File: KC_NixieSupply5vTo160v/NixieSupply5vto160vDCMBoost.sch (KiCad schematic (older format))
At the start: 47 parts, among them J1 Screw_Terminal_1x04, J2 CONN_01X01, J3 CONN_01X01, J4 CONN_01X01, J5 CONN_01X01, P1 USB_OTG, Q1 FDS2672CT, Q26 MMBTA42, U1 UCC3803

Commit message: Flyback Efficiency Calculations
Added a Efficiency calculations for a flyback converter using similar
parts, but with an off the self 8.5uH 1:5 turns ration flyback
transformer.  the DCM boost still looks like the highest efficiency.
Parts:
- removed J1: Screw_Terminal_1x04, TerminalBlock_Phoenix:TerminalBlock_Phoenix_PT-3.5mm_4pol, symbol Screw_Terminal_1x04
- removed P1: USB_OTG, NixieSupply5vto160vDCMBoost_socket:USB_Micro-B_Wurth_3A_Non-OVAL-Drill, symbol USB_OTG-RESCUE-ETAclock
- added J1: Screw_Terminal_01x04, TerminalBlock_Phoenix:TerminalBlock_Phoenix_PT-3.5mm_4pol, symbol Screw_Terminal_01x04
- added P1: USB_OTG, NixieSupply5vto160vDCMBoost_socket:USB_Micro-B_Wurth_3A_Non-OVAL-Drill, symbol USB_OTG
- J2, J3, J4, J5: symbol CONN_01X01 -> Conn_01x01
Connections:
- wire segments 161 -> 125

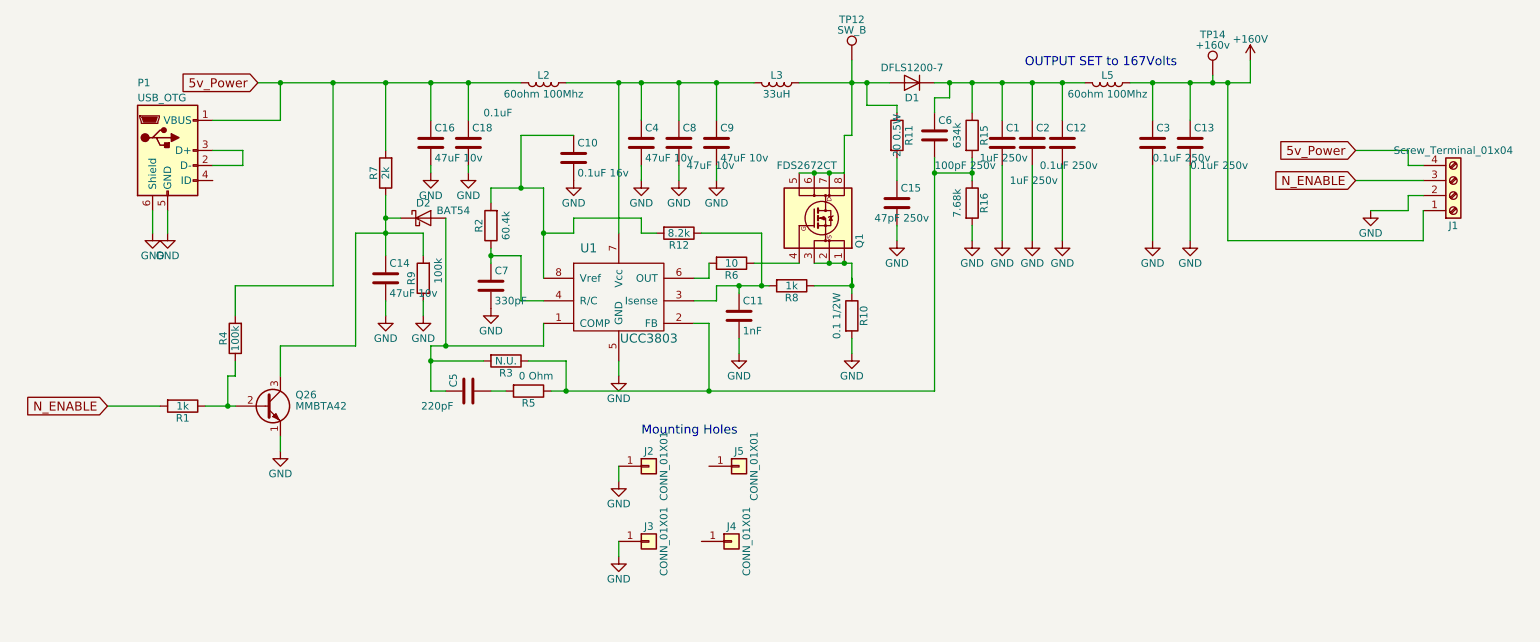
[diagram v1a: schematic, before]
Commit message: Latest updates for the verification Blog
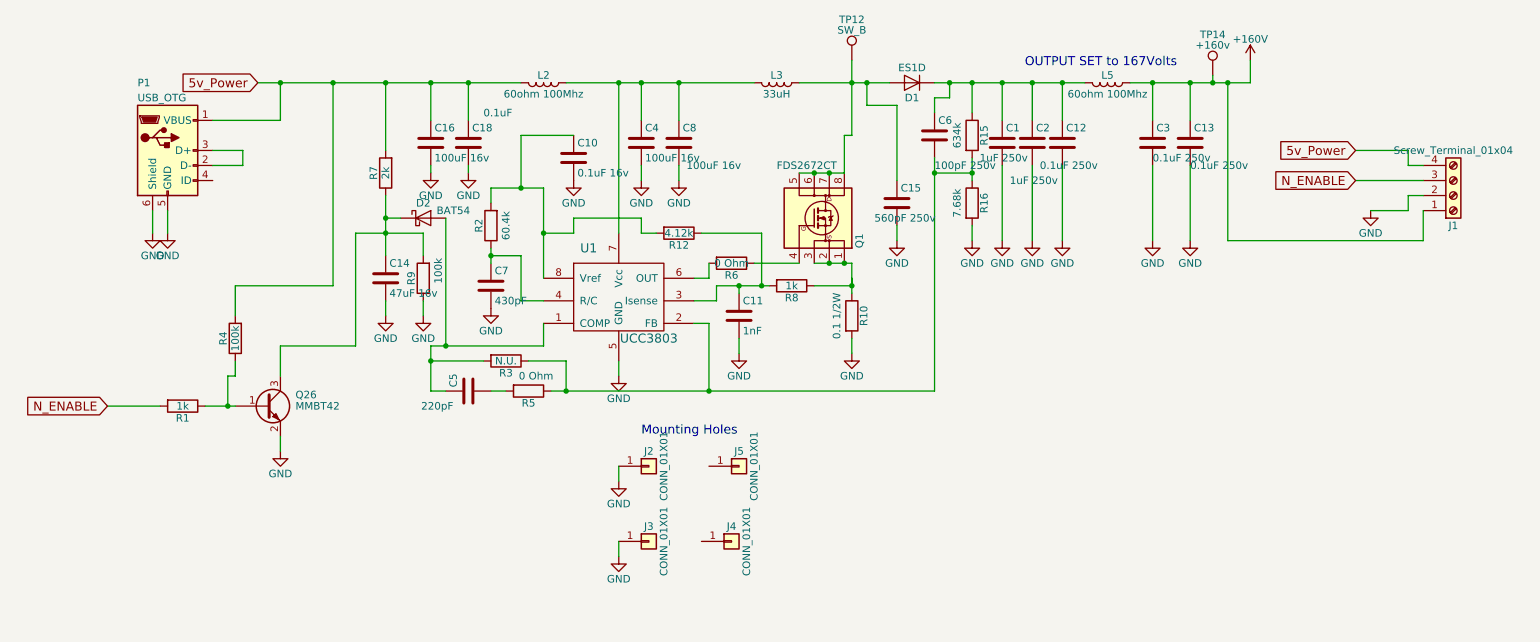
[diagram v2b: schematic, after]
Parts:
- removed C9: 47uF 10v, Capacitors_SMD:C_0805, symbol C
- removed Q26: MMBTA42, TO_SOT_Packages_SMD:SOT-23, symbol MPSA42
- removed R11: 20 0.5W, Resistors_SMD:R_0805, symbol R
- added Q26: MMBT42, TO_SOT_Packages_SMD:SOT-23, symbol MMBT3904
- C12, C13, C3, C6: MPN (none) -> CGA4J3X7T2E104M125AE
- C14: value 47uF 10v -> 47uF 16v; footprint Capacitors_SMD:C_0805 -> Capacitors_SMD:C_1206; MPN GRM21BR61A476ME15L -> C3216JB1C476M160AB
- C15: value 47pF 250v -> 560pF 250v; MPN C1608C0G2E331J080AA -> C0603C561JAGAC7867
- C16, C4, C8: value 47uF 10v -> 100uF 16v; footprint Capacitors_SMD:C_0805 -> Capacitors_SMD:C_1210; MPN GRM21BR61A476ME15L -> EMK325ABJ107MM-P
- C7: value 330pF -> 430pF; MPN (none) -> CL21C431JBANNNC
- D1: value DFLS1200-7 -> ES1D; footprint Diodes_SMD:D_PowerDI-123 -> Diodes_SMD:D_SMA_Handsoldering; MPN DFLS1200-7 -> ES1D
- J1: MPN (none) -> 1984633
- R12: value 8.2k -> 4.12k
- R6: value 10 -> 0 Ohm
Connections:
- net GND: now also Q26.2 (E)
- net at D1.2 (A), L3.1, Q1.5 (D)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: now also C15.1
- net at R1.1, R4.1: now also Q26.1 (B)
- net at C14.1, D2.1 (K), R7.1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: now also Q26.3 (C)
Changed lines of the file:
@@
 EELAYER 25 0
 EELAYER END
-$Descr A4 11693 8268
+$Descr USLetter 11000 8500
 encoding utf-8
 Sheet 1 1
@@
 P 6550 2050
 F 0 "D1" H 6550 2150 50  0000 C CNN
-F 1 "DFLS1200-7" H 6550 1950 50  0000 C CNN
-F 2 "Diodes_SMD:D_PowerDI-123" H 6550 2050 50  0001 C CNN
-F 3 "https://www.digikey.com/product-detail/en/diodes-incorporated/DFLS1200-7/DFLS1200DITR-ND/776776" H 6550 2050 50  0001 C CNN
-F 4 "DFLS1200-7 " H 6550 2050 60  0001 C CNN "MPN"
+F 1 "ES1D" H 6550 1950 50  0000 C CNN
+F 2 "Diodes_SMD:D_SMA_Handsoldering" H 6550 2050 50  0001 C CNN
+F 3 "https://www.digikey.com/product-detail/en/on-semiconductor/ES1D/ES1DFSCT-ND/458940" H 6550 2050 50  0001 C CNN
+F 4 "ES1D" H 6550 2050 60  0001 C CNN "MPN"
 	1    6550 2050
 	-1   0    0    1
@@
 P 5350 3250
 F 0 "R6" V 5430 3250 50  0000 C CNN
-F 1 "10" V 5350 3250 50  0000 C CNN
+F 1 "0 Ohm" V 5350 3250 50  0000 C CNN
 F 2 "Resistors_SMD:R_0805" V 5280 3250 50  0001 C CNN
 F 3 "" H 5350 3250 50  0000 C CNN
@@
 $EndComp
 $Comp
-L R R11
-U 1 1 58854C64
-P 6450 2400
-F 0 "R11" V 6530 2400 50  0000 C CNN
-F 1 "20 0.5W" V 6450 2400 50  0000 C CNN
-F 2 "Resistors_SMD:R_0805" V 6380 2400 50  0001 C CNN
-F 3 "" H 6450 2400 50  0001 C CNN
-	1    6450 2400
-	1    0    0    -1
-$EndComp
-$Comp
 L C C15
 U 1 1 58854D96
 P 6450 2850
 F 0 "C15" H 6475 2950 50  0000 L CNN
-F 1 "47pF 250v" H 6300 2750 50  0000 L CNN
+F 1 "560pF 250v" H 6300 2750 50  0000 L CNN
 F 2 "Capacitors_SMD:C_0603" H 6488 2700 50  0001 C CNN
-F 3 "http://www.digikey.com/product-detail/en/tdk-corporation/C1608C0G2E331J080AA/445-2317-1-ND/789826" H 6450 2850 50  0001 C CNN
-F 4 "C1608C0G2E331J080AA" H 6450 2850 60  0001 C CNN "MPN"
+F 3 "https://www.digikey.com/product-detail/en/kemet/C0603C561JAGAC7867/399-14990-1-ND/7382539" H 6450 2850 50  0001 C CNN
+F 4 "C0603C561JAGAC7867" H 6450 2850 60  0001 C CNN "MPN"
 	1    6450 2850
 	1    0    0    -1
@@
 P 3750 3400
 F 0 "C7" H 3775 3500 50  0000 L CNN
-F 1 "330pF" H 3775 3300 50  0000 L CNN
+F 1 "430pF" H 3775 3300 50  0000 L CNN
 F 2 "Capacitors_SMD:C_0805" H 3788 3250 50  0001 C CNN
-F 3 "" H 3750 3400 50  0000 C CNN
+F 3 "https://www.digikey.com/product-detail/en/samsung-electro-mechanics/CL21C431JBANNNC/1276-2659-1-ND/3890745" H 3750 3400 50  0001 C CNN
+F 4 "CL21C431JBANNNC" H 3750 3400 60  0001 C CNN "MPN"
 	1    3750 3400
 	1    0    0    -1
@@
 F 1 "100pF 250v" H 6700 2200 50  0000 L CNN
 F 2 "Capacitors_SMD:C_0805" H 6738 2250 50  0001 C CNN
-F 3 "" H 6700 2400 50  0000 C CNN
+F 3 "https://www.digikey.com/scripts/DkSearch/dksus.dll?Detail&itemSeq=248804877&uq=636513106927966714" H 6700 2400 50  0001 C CNN
+F 4 "CGA4J3X7T2E104M125AE" H 6700 2400 60  0001 C CNN "MPN"
 	1    6700 2400
 	1    0    0    -1
@@
 Connection ~ 6950 2650
 Wire Wire Line
-	6450 2700 6450 2550
-Wire Wire Line
-	6450 2200 6450 2250
+	6450 2200 6450 2700
 Wire Wire Line
 	6250 2200 6450 2200
@@
 	5000 2600 5000 2700
 $Comp
-L C C9
-U 1 1 5A46B83F
-P 5250 2450
-F 0 "C9" H 5275 2550 50  0000 L CNN
-F 1 "47uF 10v" H 5275 2350 50  0000 L CNN
-F 2 "Capacitors_SMD:C_0805" H 5288 2300 50  0001 C CNN
-F 3 "http://www.digikey.com/product-detail/en/murata-electronics-north-america/GRM21BR61A476ME15L/490-9961-1-ND/5026442" H 5250 2450 50  0001 C CNN
-F 4 "GRM21BR61A476ME15L" H 5250 2450 60  0001 C CNN "MPN"
-	1    5250 2450
-	1    0    0    -1
-$EndComp
-Wire Wire Line
-	5250 2300 5250 2050
-Connection ~ 5250 2050
-$Comp
-L GND #PWR023
-U 1 1 5A46B995
-P 5250 2700
-F 0 "#PWR023" H 5250 2450 50  0001 C CNN
-F 1 "GND" H 5250 2550 50  0000 C CNN
-F 2 "" H 5250 2700 50  0000 C CNN
-F 3 "" H 5250 2700 50  0000 C CNN
-	1    5250 2700
-	1    0    0    -1
-$EndComp
-Wire Wire Line
-	5250 2600 5250 2700
-$Comp
 L Conn_01x01 J5
 U 1 1 5A46B464
@@
 	4600 5200 4600 5100
 $Comp
-L GND #PWR024
+L GND #PWR023
 U 1 1 5A47271C
 P 4600 5200
-F 0 "#PWR024" H 4600 4950 50  0001 C CNN
+F 0 "#PWR023" H 4600 4950 50  0001 C CNN
 F 1 "GND" H 4600 5050 50  0000 C CNN
 F 2 "" H 4600 5200 50  0000 C CNN
@@
 $EndComp
 $Comp
-L GND #PWR025
+L GND #PWR024
 U 1 1 5A4727AE
 P 4600 4700
-F 0 "#PWR025" H 4600 4450 50  0001 C CNN
+F 0 "#PWR024" H 4600 4450 50  0001 C CNN
 F 1 "GND" H 4600 4550 50  0000 C CNN
 F 2 "" H 4600 4700 50  0000 C CNN
@@
 $EndComp
 $Comp
-L GND #PWR026
+L GND #PWR025
 U 1 1 5A4786FA
 P 4300 2700
-F 0 "#PWR026" H 4300 2450 50  0001 C CNN
+F 0 "#PWR025" H 4300 2450 50  0001 C CNN
 F 1 "GND" H 4300 2550 50  0000 C CNN
 F 2 "" H 4300 2700 50  0000 C CNN
@@
 P 5000 3050
 F 0 "R12" V 5080 3050 50  0000 C CNN
-F 1 "8.2k" V 5000 3050 50  0000 C CNN
+F 1 "4.12k" V 5000 3050 50  0000 C CNN
 F 2 "Resistors_SMD:R_0805" V 4930 3050 50  0001 C CNN
 F 3 "" H 5000 3050 50  0000 C CNN
@@
 F 1 "0.1uF 250v" H 8400 2300 50  0000 L CNN
 F 2 "Capacitors_SMD:C_0805" H 8438 2300 50  0001 C CNN
-F 3 "" H 8400 2450 50  0000 C CNN
+F 3 "https://www.digikey.com/product-detail/en/tdk-corporation/CGA4J3X7T2E104M125AE/445-7965-1-ND/2782533" H 8400 2450 50  0001 C CNN
+F 4 "CGA4J3X7T2E104M125AE" H 8400 2450 60  0001 C CNN "MPN"
 	1    8400 2450
 	1    0    0    -1
@@
 F 1 "0.1uF 250v" H 8150 2350 50  0000 L CNN
 F 2 "Capacitors_SMD:C_0805" H 8188 2300 50  0001 C CNN
-F 3 "" H 8150 2450 50  0000 C CNN
+F 3 "https://www.digikey.com/product-detail/en/tdk-corporation/CGA4J3X7T2E104M125AE/445-7965-1-ND/2782533" H 8150 2450 50  0001 C CNN
+F 4 "CGA4J3X7T2E104M125AE" H 8150 2450 60  0001 C CNN "MPN"
 	1    8150 2450
 	1    0    0    -1
@@
 F 1 "0.1uF 250v" H 7400 2300 50  0000 L CNN
 F 2 "Capacitors_SMD:C_0805" H 7588 2300 50  0001 C CNN
-F 3 "" H 7550 2450 50  0000 C CNN
+F 3 "https://www.digikey.com/product-detail/en/tdk-corporation/CGA4J3X7T2E104M125AE/445-7965-1-ND/2782533" H 7550 2450 50  0001 C CNN
+F 4 "CGA4J3X7T2E104M125AE" H 7550 2450 60  0001 C CNN "MPN"
 	1    7550 2450
 	1    0    0    -1
@@
 P 5000 2450
 F 0 "C8" H 5025 2550 50  0000 L CNN
-F 1 "47uF 10v" H 5050 2300 50  0000 L CNN
-F 2 "Capacitors_SMD:C_0805" H 5038 2300 50  0001 C CNN
+F 1 "100uF 16v" H 5050 2300 50  0000 L CNN
+F 2 "Capacitors_SMD:C_1210" H 5038 2300 50  0001 C CNN
 F 3 "http://www.digikey.com/product-detail/en/murata-electronics-north-america/GRM21BR61A476ME15L/490-9961-1-ND/5026442" H 5000 2450 50  0001 C CNN
-F 4 "GRM21BR61A476ME15L" H 5000 2450 60  0001 C CNN "MPN"
+F 4 "EMK325ABJ107MM-P" H 5000 2450 60  0001 C CNN "MPN"
 	1    5000 2450
 	1    0    0    -1
@@
 P 4750 2450
 F 0 "C4" H 4775 2550 50  0000 L CNN
-F 1 "47uF 10v" H 4775 2350 50  0000 L CNN
-F 2 "Capacitors_SMD:C_0805" H 4788 2300 50  0001 C CNN
+F 1 "100uF 16v" H 4775 2350 50  0000 L CNN
+F 2 "Capacitors_SMD:C_1210" H 4788 2300 50  0001 C CNN
 F 3 "http://www.digikey.com/product-detail/en/murata-electronics-north-america/GRM21BR61A476ME15L/490-9961-1-ND/5026442" H 4750 2450 50  0001 C CNN
-F 4 "GRM21BR61A476ME15L" H 4750 2450 60  0001 C CNN "MPN"
+F 4 "EMK325ABJ107MM-P" H 4750 2450 60  0001 C CNN "MPN"
 	1    4750 2450
 	1    0    0    -1
@@
 P 3350 2450
 F 0 "C16" H 3375 2550 50  0000 L CNN
-F 1 "47uF 10v" H 3375 2350 50  0000 L CNN
-F 2 "Capacitors_SMD:C_0805" H 3388 2300 50  0001 C CNN
-F 3 "http://www.digikey.com/product-detail/en/murata-electronics-north-america/GRM21BR61A476ME15L/490-9961-1-ND/5026442" H 3350 2450 50  0001 C CNN
-F 4 "GRM21BR61A476ME15L" H 3350 2450 60  0001 C CNN "MPN"
+F 1 "100uF 16v" H 3375 2350 50  0000 L CNN
+F 2 "Capacitors_SMD:C_1210" H 3388 2300 50  0001 C CNN
+F 3 "https://www.digikey.com/product-detail/en/taiyo-yuden/EMK325ABJ107MM-P/587-5426-2-ND/7067011" H 3350 2450 50  0001 C CNN
+F 4 "EMK325ABJ107MM-P" H 3350 2450 60  0001 C CNN "MPN"
 	1    3350 2450
 	1    0    0    -1
@@
 P 3050 3350
 F 0 "C14" H 3075 3450 50  0000 L CNN
-F 1 "47uF 10v" H 3075 3250 50  0000 L CNN
-F 2 "Capacitors_SMD:C_0805" H 3088 3200 50  0001 C CNN
-F 3 "http://www.digikey.com/product-detail/en/murata-electronics-north-america/GRM21BR61A476ME15L/490-9961-1-ND/5026442" H 3050 3350 50  0001 C CNN
-F 4 "GRM21BR61A476ME15L" H 3050 3350 60  0001 C CNN "MPN"
+F 1 "47uF 16v" H 3075 3250 50  0000 L CNN
+F 2 "Capacitors_SMD:C_1206" H 3088 3200 50  0001 C CNN
+F 3 "https://www.digikey.com/product-detail/en/tdk-corporation/C3216JB1C476M160AB/445-11695-1-ND/3953361" H 3050 3350 50  0001 C CNN
+F 4 "C3216JB1C476M160AB" H 3050 3350 60  0001 C CNN "MPN"
 	1    3050 3350
 	1    0    0    -1
@@
 $EndComp
 $Comp
-L MPSA42 Q26
-U 1 1 5A400D9C
-P 2250 4200
-F 0 "Q26" H 2450 4275 50  0000 L CNN
-F 1 "MMBTA42" H 2450 4200 50  0000 L CNN
-F 2 "TO_SOT_Packages_SMD:SOT-23" H 2450 4125 50  0001 L CIN
-F 3 "http://www.digikey.com/product-detail/en/micro-commercial-co/MMBTA42-TP/MMBTA42TPMSCT-ND/717401" H 2250 4200 50  0001 L CNN
-	1    2250 4200
-	1    0    0    -1
-$EndComp
-$Comp
 L USB_OTG P1
 U 1 1 5A51695C
@@
 F 1 "Screw_Terminal_01x04" H 10150 2500 50  0000 C CNN
 F 2 "TerminalBlock_Phoenix:TerminalBlock_Phoenix_PT-3.5mm_4pol" H 10150 2800 50  0001 C CNN
-F 3 "" H 10150 2800 50  0001 C CNN
+F 3 "https://www.digikey.com/scripts/DkSearch/dksus.dll?Detail&itemSeq=248943251&uq=636514658010412978" H 10150 2800 50  0001 C CNN
+F 4 "1984633" H 10150 2800 60  0001 C CNN "MPN"
 	1    10150 2800
 	1    0    0    1
@@
 Wire Wire Line
 	9950 3100 9950 2900
+$Comp
+L MMBT3904 Q26
+U 1 1 5A6EF5F8
+P 2250 4200
+F 0 "Q26" H 2450 4275 50  0000 L CNN
+F 1 "MMBT42" H 2450 4200 50  0000 L CNN
+F 2 "TO_SOT_Packages_SMD:SOT-23" H 2450 4125 50  0001 L CIN
+F 3 "http://www.digikey.com/product-detail/en/micro-commercial-co/MMBTA42-TP/MMBTA42TPMSCT-ND/717401" H 2250 4200 50  0001 L CNN
+	1    2250 4200
+	1    0    0    -1
+$EndComp
 $EndSCHEMATC
